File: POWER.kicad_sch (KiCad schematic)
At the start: 0 parts

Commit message: 80% done, maybe add more AINs, finish the power circuit and add system & block diagrams
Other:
- note added: "Power Section"
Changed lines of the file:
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@@
 		(company "Elnady Electronics")
 	)
+	(text "Power Section"
+		(exclude_from_sim no)
+		(at 56.134 22.606 0)
+		(effects
+			(font
+				(size 6 6)
+				(thickness 1.2)
+				(bold yes)
+			)
+		)
+	)
 )

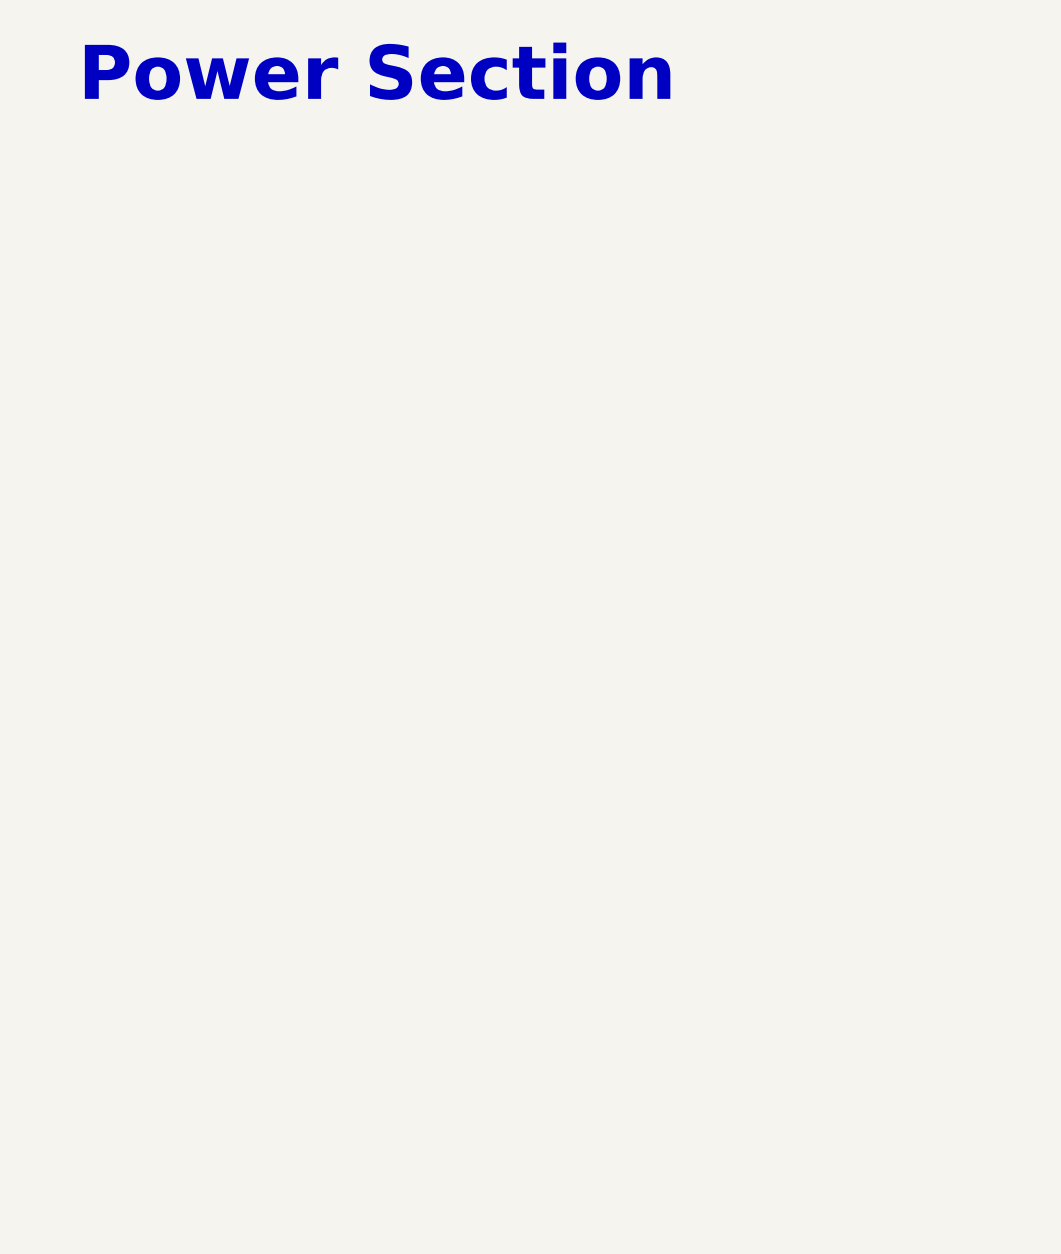
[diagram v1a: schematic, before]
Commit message: finished individual block placement and started integrating, might need to change the AFEs length
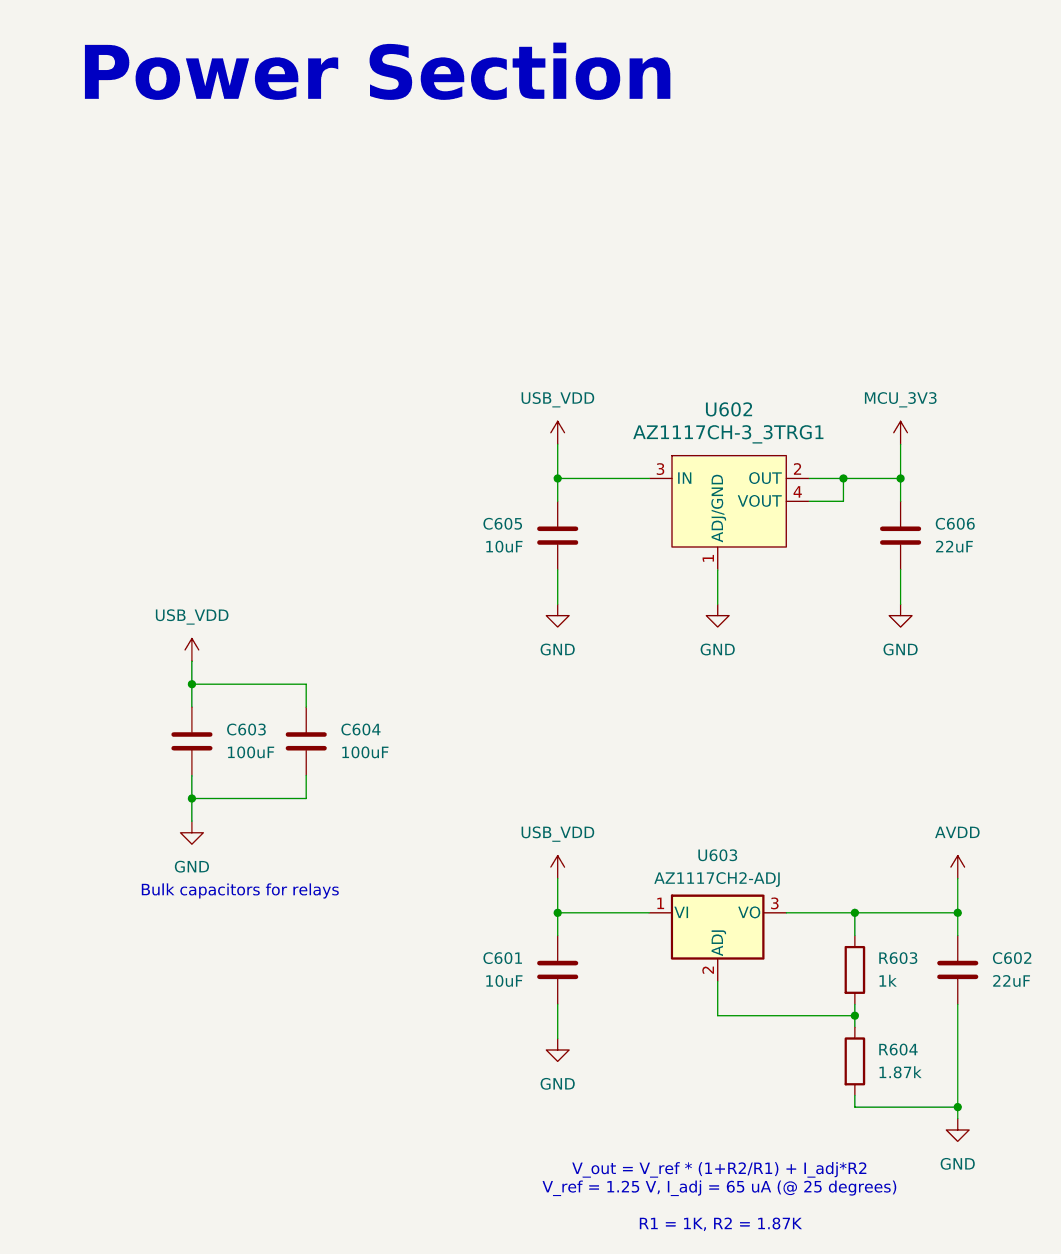
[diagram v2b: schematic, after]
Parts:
- added C601, C605: 10uF, Capacitor_SMD:C_0805_2012Metric, symbol Device:C
- added C602, C606: 22uF, Capacitor_SMD:C_0805_2012Metric, symbol Device:C
- added C603, C604: 100uF, Capacitor_SMD:C_1206_3216Metric, symbol Device:C
- added R603: 1k, Resistor_SMD:R_0603_1608Metric, symbol Device:R
- added R604: 1.87k, Resistor_SMD:R_0603_1608Metric, symbol Device:R
- added U602: AZ1117CH-3_3TRG1, digikey-footprints:SOT-223, symbol dk_PMIC-Voltage-Regulators-Linear:AZ1117CH-3_3TRG1
- added U603: AZ1117CH2-ADJ, Package_TO_SOT_SMD:SOT-223-3_TabPin2, symbol Regulator_Linear:AZ1117CH2-ADJ
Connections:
- new net: R603.2, R604.1, U603.2 (ADJ)
- new net AVDD: C602.1, R603.1, U603.3 (VO)
- new net GND: C601.2, C602.2, C603.2, C604.2, C605.2, C606.2, R604.2, U602.1 (ADJ/GND)
- new net MCU_3V3: C606.1, U602.2 (OUT), U602.4 (VOUT)
- new net USB_VDD: C601.1, C603.1, C604.1, C605.1, U602.3 (IN), U603.1 (VI)
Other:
- note added: "Bulk capacitors for relays"
- note added: "V_out = V_ref * (1+R2/R1) + I_adj*R2 V_ref = 1.25 V, I_adj = 65 uA (@ 25 degrees) R1 = 1K, R2 = 1.87K"
